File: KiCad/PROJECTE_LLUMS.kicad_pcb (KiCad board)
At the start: 2 copper layers, 100 x 55.4 mm, 65 parts, among them J1 CONNECTOR_MOTOR, J3 Conn_01x03, J4 Conn_01x02_Pin, J5 DE9_Pins, Q2 IRLZ44N, Q3 IRLZ44N, Q4 IRLZ44N, Q5 IRLZ44N, Q6 IRLZ44N, Q7 IRLZ44N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

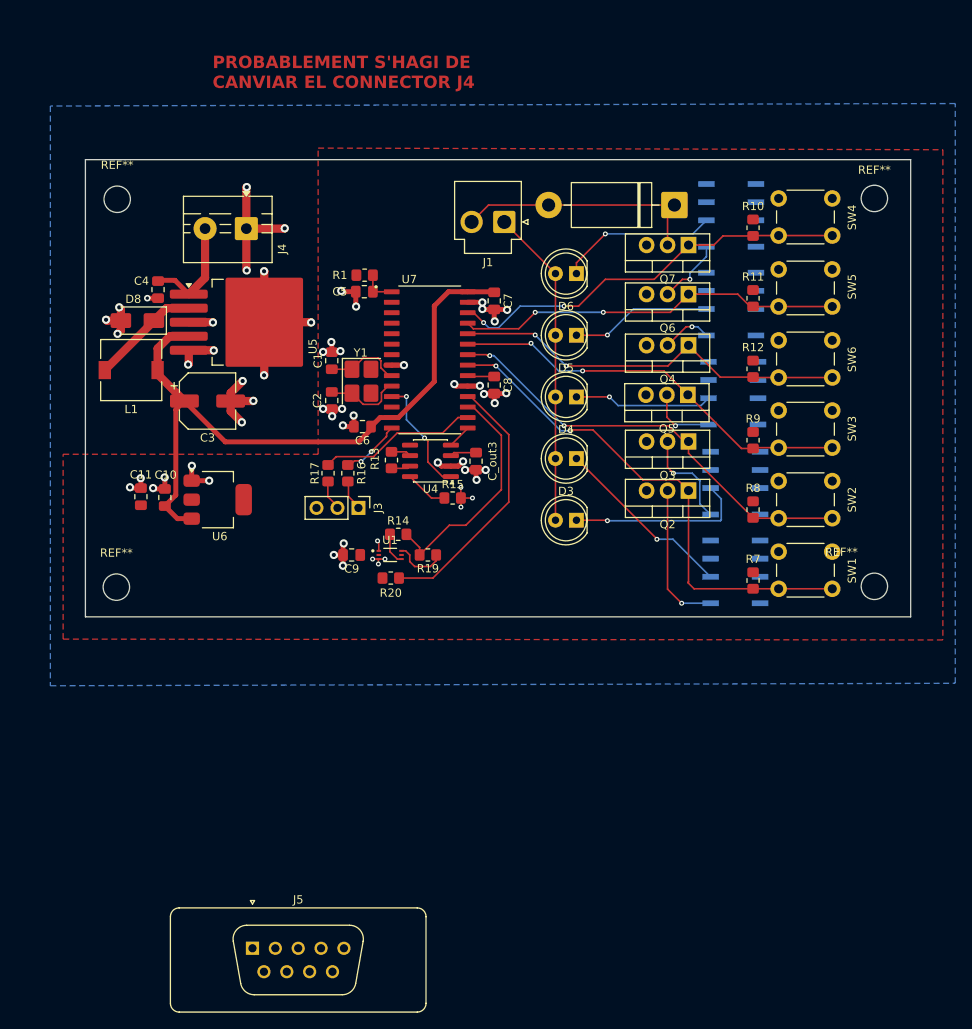
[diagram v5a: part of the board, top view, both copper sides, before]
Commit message: alguns errors de CADLAB i he canivat d'ordre els LEDs i els drivers a la PCB.
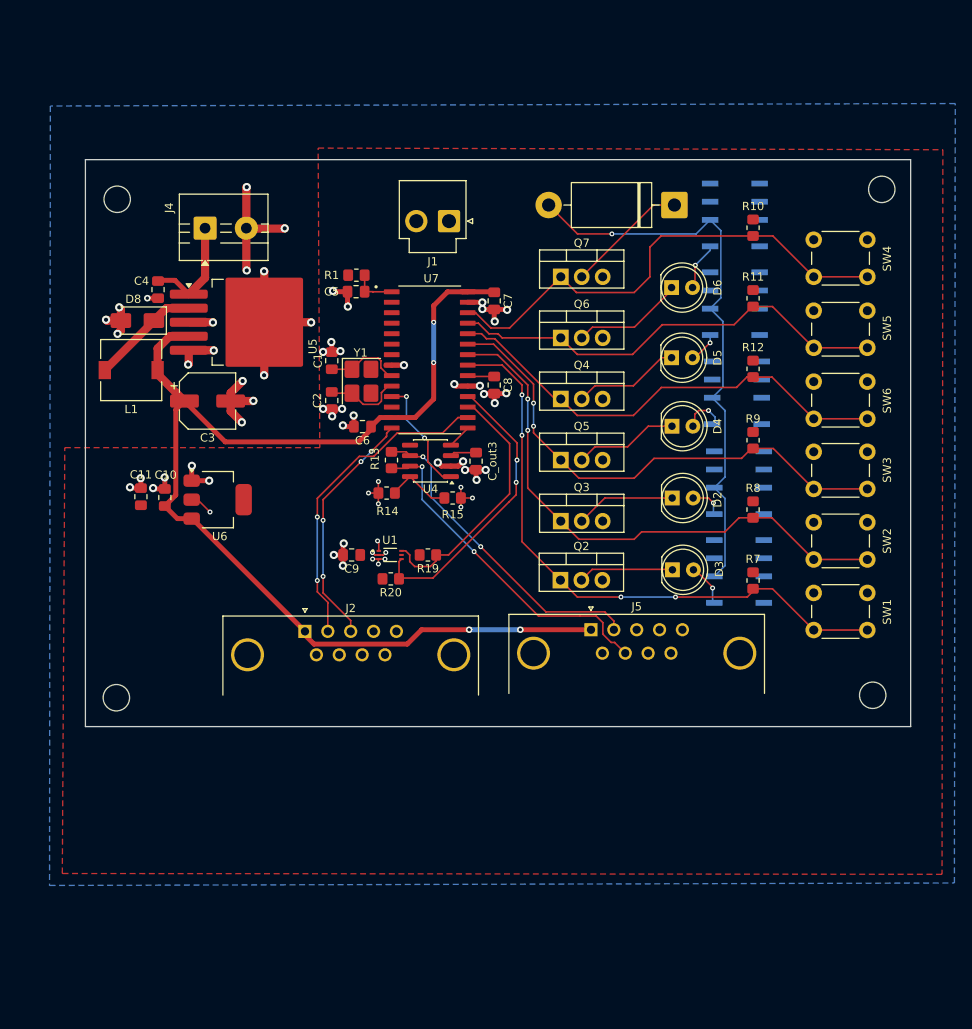
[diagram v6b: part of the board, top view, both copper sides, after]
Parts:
- removed J3: Conn_01x03, Connector_PinHeader_2.54mm:PinHeader_1x03_P2.54mm_Vertical
- removed R16, R17: 100, Resistor_SMD:R_0805_2012Metric_Pad1.20x1.40mm_HandSolder
- added J2: DE9_Pins_MountingHoles, Connector_Dsub:DSUB-9_Pins_Horizontal_P2.77x2.84mm_EdgePinOffset4.94mm_Housed_MountingHolesOffset4.94mm, F.Cu at (109.6, 125.7)
- J5: value DE9_Pins -> DE9_Pins_MountingHoles; footprint Connector_Dsub:DSUB-9_Pins_Vertical_P2.77x2.84mm -> Connector_Dsub:DSUB-9_Pins_Horizontal_P2.77x2.84mm_EdgePinOffset4.94mm_Housed_MountingHolesOffset4.94mm
- R14: value 4.7k -> 10k
- moved J5 56.3 mm to (144.3, 125.5)
- moved Q2 18.9 mm to (140.6, 119.5), turned to 0 degrees
- moved Q3 18.2 mm to (140.6, 112.3), turned to 0 degrees
- moved D3 17.8 mm to (154.1, 118.2), turned to 0 degrees
- moved Q5 17.3 mm to (140.6, 104.9), turned to 0 degrees
- moved Q4 16.8 mm to (140.6, 97.5), turned to 0 degrees
- moved Q6 16.4 mm to (140.6, 90.1), turned to 0 degrees
- moved Q7 16.0 mm to (140.6, 82.7), turned to 0 degrees
- moved REF** 13.4 mm to (86.8, 133.7)
- moved REF** 13.2 mm to (178.4, 133.4)
- moved D4 12.1 mm to (154.1, 100.8), turned to 0 degrees
- moved D2 11.9 mm to (154.1, 109.5), turned to 0 degrees
- moved D5 11.8 mm to (154.0, 92.5), turned to 0 degrees
- moved D6 11.6 mm to (154.0, 84.0), turned to 0 degrees
- moved J1 6.70 mm to (127.1, 76.0)
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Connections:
- C10 pad 1: 5V -> +5V
- C11 pad 1: 3V3 -> +3V3
- C3 pad 1: 5V -> +5V
- C6 pad 1: 5V -> +5V
- C7 pad 1: 5V -> +5V
- C9 pad 1: 3V3 -> +3V3
- D2 pad 1: Net-(D2-K) -> /llums/C_LED2
- D2 pad 2: +12V -> /llums/A_LED2
- D3 pad 1: Net-(D3-K) -> /llums/C_LED3
- D3 pad 2: +12V -> /llums/A_LED3
- D4 pad 1: Net-(D4-K) -> /llums/C_LED4
- D4 pad 2: +12V -> /llums/A_LED4
- D5 pad 1: Net-(D5-K) -> /llums/C_LED5
- D5 pad 2: +12V -> /llums/A_LED5
- D6 pad 1: Net-(D6-K) -> /llums/C_LED6
- D6 pad 2: +12V -> /llums/A_LED6
- D7 pad 1: Net-(D7-A) -> /llums/RELÉ
- D7 pad 2: Net-(D7-A) -> +12V
- J1 pad 1: +12V -> /llums/MOTOR
- J1 pad 2: Net-(D7-A) -> GND
- J4 pad 1: GND -> /alimentacio/12V
- J4 pad 2: /alimentacio/12V -> GND
- J5 pad 1: GND -> +5V
- J5 pad 2: unconnected-(J5-Pad2) -> /transciever/CANL
- J5 pad 3: /transciever/CANH -> unconnected-(J5-Pad3)
- J5 pad 5: UART_TX -> GND
- J5 pad 7: /transciever/CANL -> /transciever/CANH
- J5 pad 9: UART_RX -> unconnected-(J5-Pad9)
- L1 pad 2: 5V -> +5V
- Q2 pad 2: Net-(Q2-D) -> /llums/C_LED3
- Q3 pad 2: Net-(Q3-D) -> /llums/C_LED2
- Q4 pad 2: Net-(Q4-D) -> /llums/C_LED5
- Q5 pad 2: Net-(Q5-D) -> /llums/C_LED4
- Q6 pad 2: Net-(Q6-D) -> /llums/C_LED6
- Q7 pad 2: Net-(D7-A) -> /llums/RELÉ
- R1 pad 2: 3V3 -> +3V3
- R10 pad 1: 3V3 -> +3V3
- R11 pad 1: 3V3 -> +3V3
- R12 pad 1: 3V3 -> +3V3
- R14 pad 1: /sensor_llum/SDA -> /transciever/Rs
- R14 pad 2: 3V3 -> GND
- R19 pad 1: /sensor_llum/SCL -> I2C_SCL
- R19 pad 2: 3V3 -> +3V3
- R2 pad 1: Net-(Q3-D) -> /llums/A_LED2
- R2 pad 2: Net-(D2-K) -> +12V
- R20 pad 1: 3V3 -> I2C_SDA
- R20 pad 2: I2C_SDA -> +3V3
- R3 pad 1: Net-(Q2-D) -> /llums/A_LED3
- R3 pad 2: Net-(D3-K) -> +12V
- R4 pad 1: Net-(Q5-D) -> /llums/A_LED4
- R4 pad 2: Net-(D4-K) -> +12V
- R5 pad 1: Net-(Q4-D) -> /llums/A_LED5
- R5 pad 2: Net-(D5-K) -> +12V
- R6 pad 1: Net-(Q6-D) -> /llums/A_LED6
- R6 pad 2: Net-(D6-K) -> +12V
- R7 pad 1: 3V3 -> +3V3
- R8 pad 1: 3V3 -> +3V3
- R9 pad 1: 3V3 -> +3V3
- U1 pad 1: 3V3 -> +3V3
- U1 pad 4: /sensor_llum/SDA -> I2C_SDA
- U1 pad 6: /sensor_llum/SCL -> I2C_SCL
- U5 pad 4: 5V -> +5V
- U6 pad 2: 3V3 -> +3V3
- U6 pad 3: 5V -> +5V
- U7 pad 13: 5V -> +5V
- U7 pad 17: 3V3 -> I2C_SCL
- U7 pad 18: 3V3 -> I2C_SDA
- U7 pad 28: 5V -> +5V
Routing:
- net +5V: track 0.00 -> 139.1 mm, vias 0 -> 4
- net 5V: track 82.4 -> 0.00 mm
- net /transciever/CANH: track 3.26 -> 41.9 mm, vias 0 -> 2
- net /transciever/CANL: track 2.79 -> 39.1 mm, vias 0 -> 2
- net I2C_SCL: track 0.00 -> 31.4 mm
- net +12V: track 38.7 -> 69.4 mm, vias 0 -> 1
- net Net-(D7-A): track 30.6 -> 0.00 mm
- net 3V3: track 30.4 -> 0.00 mm, vias 1 -> 0
- net Net-(D3-K): track 22.2 -> 0.00 mm, vias 1 -> 0
- net UART_TX: track 7.39 -> 29.6 mm, vias 2 -> 4
- net Net-(D2-K): track 22.0 -> 0.00 mm, vias 1 -> 0
- net UART_RX: track 19.3 -> 39.0 mm, vias 0 -> 2
- net Net-(D6-K): track 19.2 -> 0.00 mm, vias 1 -> 0
- net Net-(Q2-D): track 17.9 -> 0.00 mm, vias 1 -> 0
- net Net-(D5-K): track 17.1 -> 0.00 mm, vias 1 -> 0
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- added copper zone on F.Cu, net +3V3
- removed copper zone on F.Cu, net 3V3
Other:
- board size 100 x 55.4 mm -> 100 x 68.7 mm
- board text removed: "PROBABLEMENT S'HAGI DE CANVIAR EL CONNECTOR J4"

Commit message: modificacions cadlab
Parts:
- removed R15: 10k, Resistor_SMD:R_0805_2012Metric_Pad1.20x1.40mm_HandSolder
- U7: value PIC24HJ128GP502-I_SO -> ~; footprint footprints:SOIC127P1030X265-28N -> projecte_llums:SOIC127P1030X265-28N
- moved R14 8.22 mm to (127.7, 109.4), turned to 0 degrees
- moved J5 0.21 mm to (144.3, 125.7)
- moved U7 0.10 mm to (124.8, 92.7)
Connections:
- net /microcontrolador/VCAP renamed Net-(U7-VCAP)
- net /transciever/CANH renamed /microcontrolador/CANH
- net /transciever/CANL renamed /microcontrolador/CANL
- net /transciever/Rs renamed /microcontrolador/Rs
- net Net-(U4-VDD) renamed /microcontrolador/VDD
- U7 pad 6: PMW -> unconnected-(U7-PMW-Pad6)
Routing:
- net GND: track 117.0 -> 113.1 mm, vias 61 -> 58
- net /microcontrolador/Rs: track 7.59 -> 5.24 mm
- net +5V: track 139.1 -> 139.3 mm, vias 4 -> 2

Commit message: Relé??
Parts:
- moved REF** 3.70 mm to (86.8, 130.0)
- moved REF** 2.90 mm to (178.4, 130.5)
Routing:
- net +5V: track 139.3 -> 139.4 mm, vias 2 -> 4
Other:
- board size 100 x 68.7 mm -> 100 x 65.2 mm
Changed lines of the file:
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@@
 	(footprint "MountingHole:MountingHole_3.2mm_M3"
 		(layer "F.Cu")
-		(at 86.75 133.7)
+		(at 86.75 130)
 		(descr "Mounting Hole 3.2mm, M3, no annular, generated by kicad-footprint-generator mountinghole.py")
 		(tags "mountinghole M3")
@@
 	(footprint "MountingHole:MountingHole_3.2mm_M3"
 		(layer "F.Cu")
-		(at 178.4 133.4)
+		(at 178.4 130.5)
 		(descr "Mounting Hole 3.2mm, M3, no annular, generated by kicad-footprint-generator mountinghole.py")
 		(tags "mountinghole M3")
@@
 	(gr_rect
 		(start 83 68.5)
-		(end 183 137.2)
+		(end 183 133.7)
 		(stroke
 			(width 0.05)
@@
 	)
 	(segment
+		(start 102.7 102.7)
+		(end 102.75 102.75)
+		(width 0.6)
+		(layer "F.Cu")
+		(net 3)
+	)
+	(segment
 		(start 129.5 125.46)
 		(end 123.74 125.46)
@@
 	)
 	(segment
-		(start 99.95 102.7)
-		(end 116.1 102.7)
-		(width 0.6)
-		(layer "F.Cu")
-		(net 3)
-	)
-	(segment
 		(start 93.225 89.9)
 		(end 95.525 89.9)
@@
 	)
 	(segment
+		(start 99.95 102.7)
+		(end 102.7 102.7)
+		(width 0.6)
+		(layer "F.Cu")
+		(net 3)
+	)
+	(segment
 		(start 95.945 112)
 		(end 109.605 125.66)
@@
 	)
 	(via
+		(at 102.75 102.75)
+		(size 0.6)
+		(drill 0.3)
+		(layers "F.Cu" "B.Cu")
+		(net 3)
+	)
+	(via
 		(at 129.5 125.46)
 		(size 0.8)
@@
 		(net 3)
 	)
+	(via
+		(at 116.1 102.7)
+		(size 0.6)
+		(drill 0.3)
+		(layers "F.Cu" "B.Cu")
+		(net 3)
+	)
+	(segment
+		(start 102.75 102.75)
+		(end 116.05 102.75)
+		(width 0.6)
+		(layer "B.Cu")
+		(net 3)
+	)
 	(segment
 		(start 129.5 125.46)
@@
 	)
 	(segment
+		(start 116.05 102.75)
+		(end 116.1 102.7)
+		(width 0.6)
+		(layer "B.Cu")
+		(net 3)
+	)
+	(segment
 		(start 112.375 122.225)
 		(end 112.41645 122.18355)
@@
 		(polygon
 			(pts
-				(xy 186.9 67.3) (xy 186.8 155.1) (xy 80.2 155) (xy 80.5 103.4) (xy 111.4 103.4) (xy 111.2 67.1)
+				(xy 186.9 67.3) (xy 186.8 155.1) (xy 80.2 155) (xy 80.5 103.4) (xy 110.9 103.4) (xy 110.7 67.1)
 			)
 		)
